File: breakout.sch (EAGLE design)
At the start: 26 parts

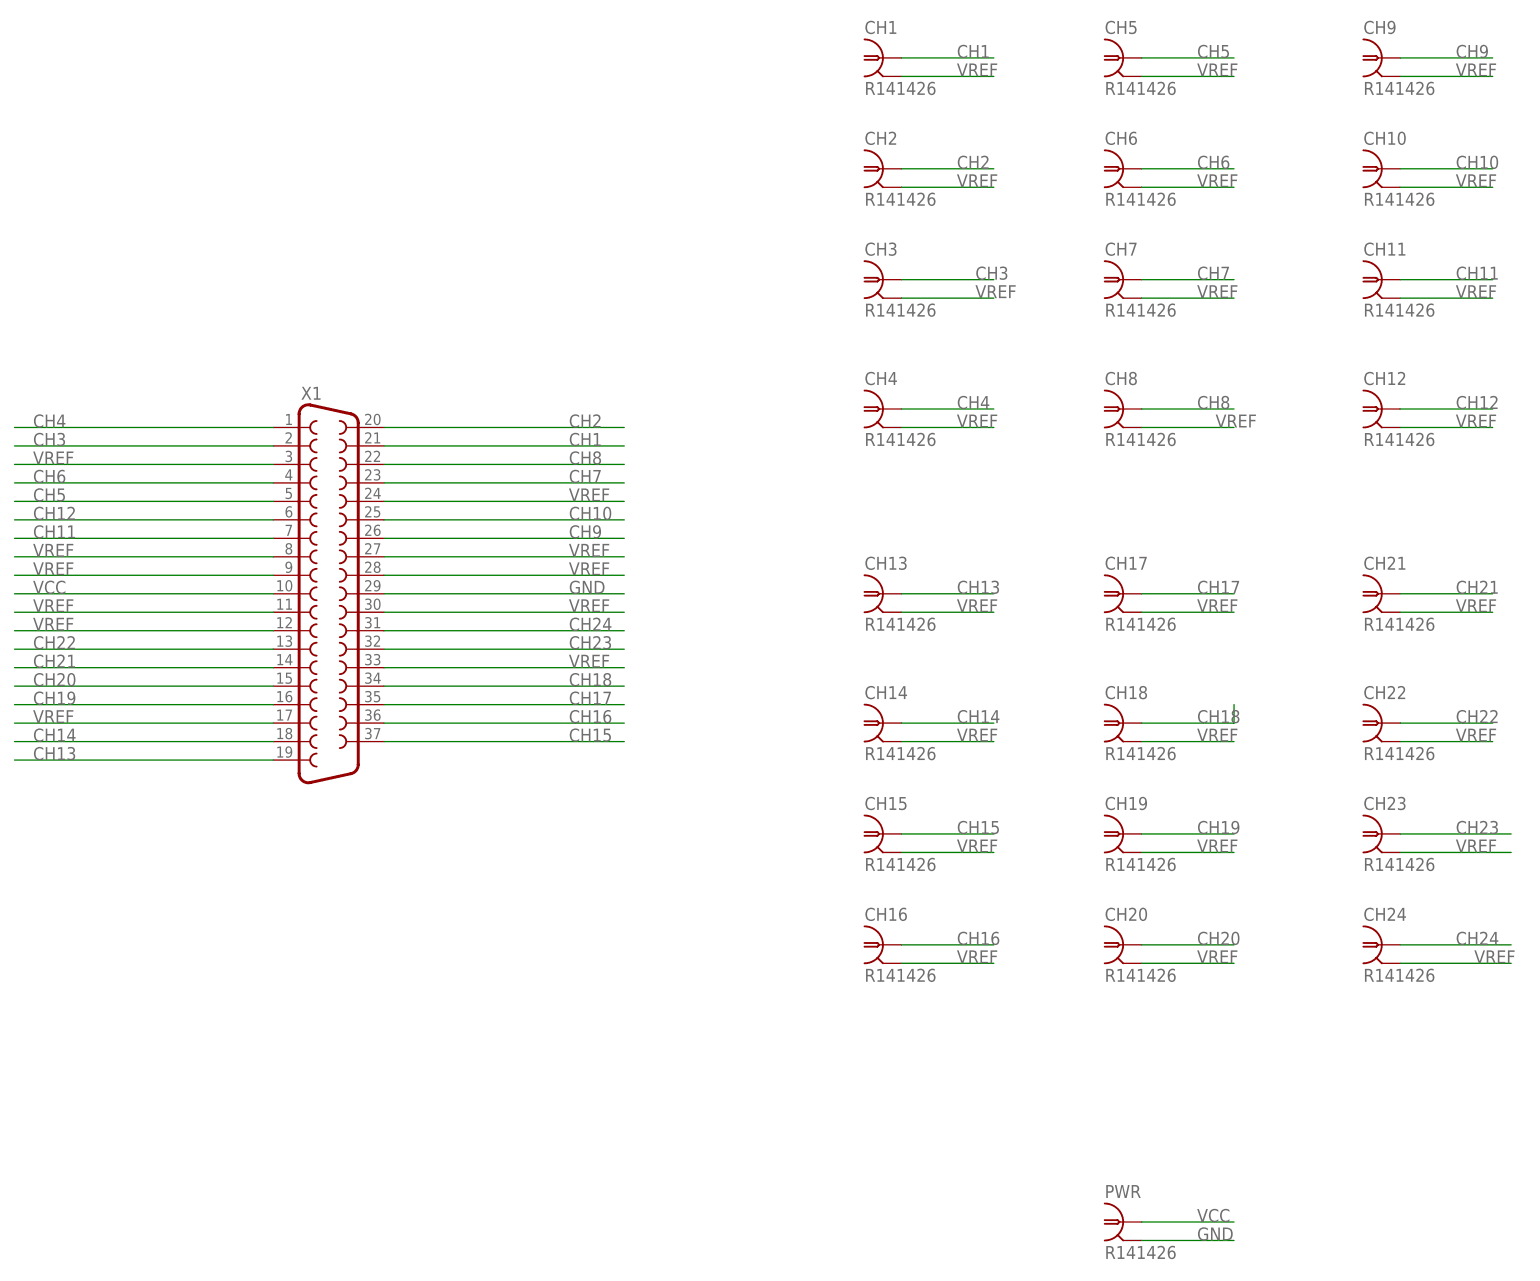
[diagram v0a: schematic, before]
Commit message: minor labeling and component placement updates. most significant is correcting part position on powerboard so 22uF bypass cap actually connects to ground.
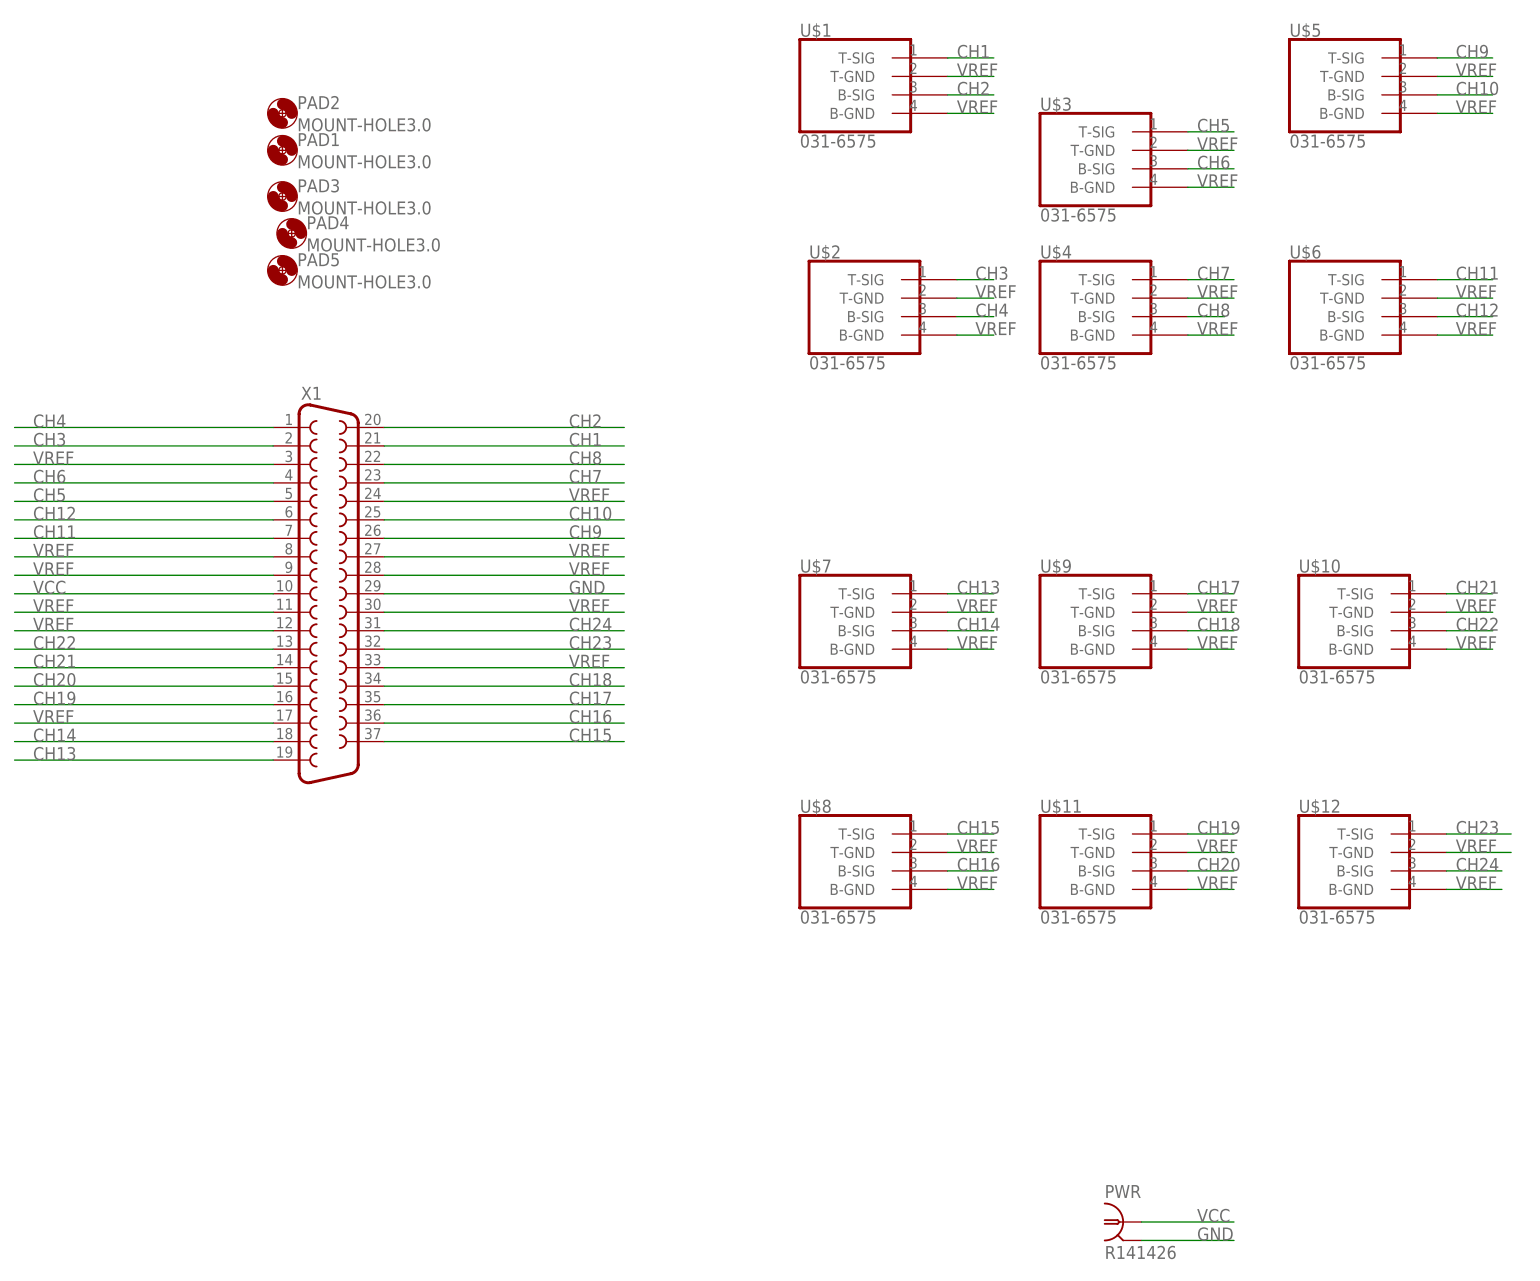
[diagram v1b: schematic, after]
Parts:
- removed CH1, CH10, CH11, CH12, CH13, CH14, CH15, CH16, CH17, CH18, CH19, CH2, CH20, CH21, CH22, CH23, CH24, CH3, CH4, CH5, CH6, CH7, CH8, CH9: R141426, con-coax:R141426
- added PAD1, PAD2, PAD3, PAD4, PAD5: MOUNT-HOLE3.0, holes:MOUNT-HOLE3.0
- added U$1, U$10, U$11, U$12, U$2, U$3, U$4, U$5, U$6, U$7, U$8, U$9: 031-6575, 031-6575:031-6575
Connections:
- net CH1: now also U$1.T-SIG; no longer CH1.1
- net CH10: now also U$5.B-SIG; no longer CH10.1
- net CH11: now also U$6.T-SIG; no longer CH11.1
- net CH12: now also U$6.B-SIG; no longer CH12.1
- net CH13: now also U$7.T-SIG; no longer CH13.1
- net CH14: now also U$7.B-SIG; no longer CH14.1
- net CH15: now also U$8.T-SIG; no longer CH15.1
- net CH16: now also U$8.B-SIG; no longer CH16.1
- net CH17: now also U$9.T-SIG; no longer CH17.1
- net CH18: now also U$9.B-SIG; no longer CH18.1
- net CH19: now also U$11.T-SIG; no longer CH19.1
- net CH2: now also U$1.B-SIG; no longer CH2.1
- net CH20: now also U$11.B-SIG; no longer CH20.1
- net CH21: now also U$10.T-SIG; no longer CH21.1
- net CH22: now also U$10.B-SIG; no longer CH22.1
- net CH23: now also U$12.T-SIG; no longer CH23.1
- net CH24: now also U$12.B-SIG; no longer CH24.1
- net CH3: now also U$2.T-SIG; no longer CH3.1
- net CH4: now also U$2.B-SIG; no longer CH4.1
- net CH5: now also U$3.T-SIG; no longer CH5.1
- net CH6: now also U$3.B-SIG; no longer CH6.1
- net CH7: now also U$4.T-SIG; no longer CH7.1
- net CH8: now also U$4.B-SIG; no longer CH8.1
- net CH9: now also U$5.T-SIG; no longer CH9.1
- net VREF: now also U$1.B-GND, U$1.T-GND, U$10.B-GND, U$10.T-GND, U$11.B-GND, U$11.T-GND, U$12.B-GND, U$12.T-GND, U$2.B-GND, U$2.T-GND, U$3.B-GND, U$3.T-GND, U$4.B-GND, U$4.T-GND, U$5.B-GND, U$5.T-GND, U$6.B-GND, U$6.T-GND, U$7.B-GND, U$7.T-GND, U$8.B-GND, U$8.T-GND, U$9.B-GND, U$9.T-GND; no longer CH1.2, CH10.2, CH11.2, CH12.2, CH13.2, CH14.2, CH15.2, CH16.2, CH17.2, CH18.2, CH19.2, CH2.2, CH20.2, CH21.2, CH22.2, CH23.2, CH24.2, CH3.2, CH4.2, CH5.2, CH6.2, CH7.2, CH8.2, CH9.2
